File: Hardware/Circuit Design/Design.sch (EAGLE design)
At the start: 41 parts, among them J1 6495, U1 ATMEGA328-PU, U2 TP4056, U3 HTU21D, U4 MT3608, Y1 16 MHz HC-49US

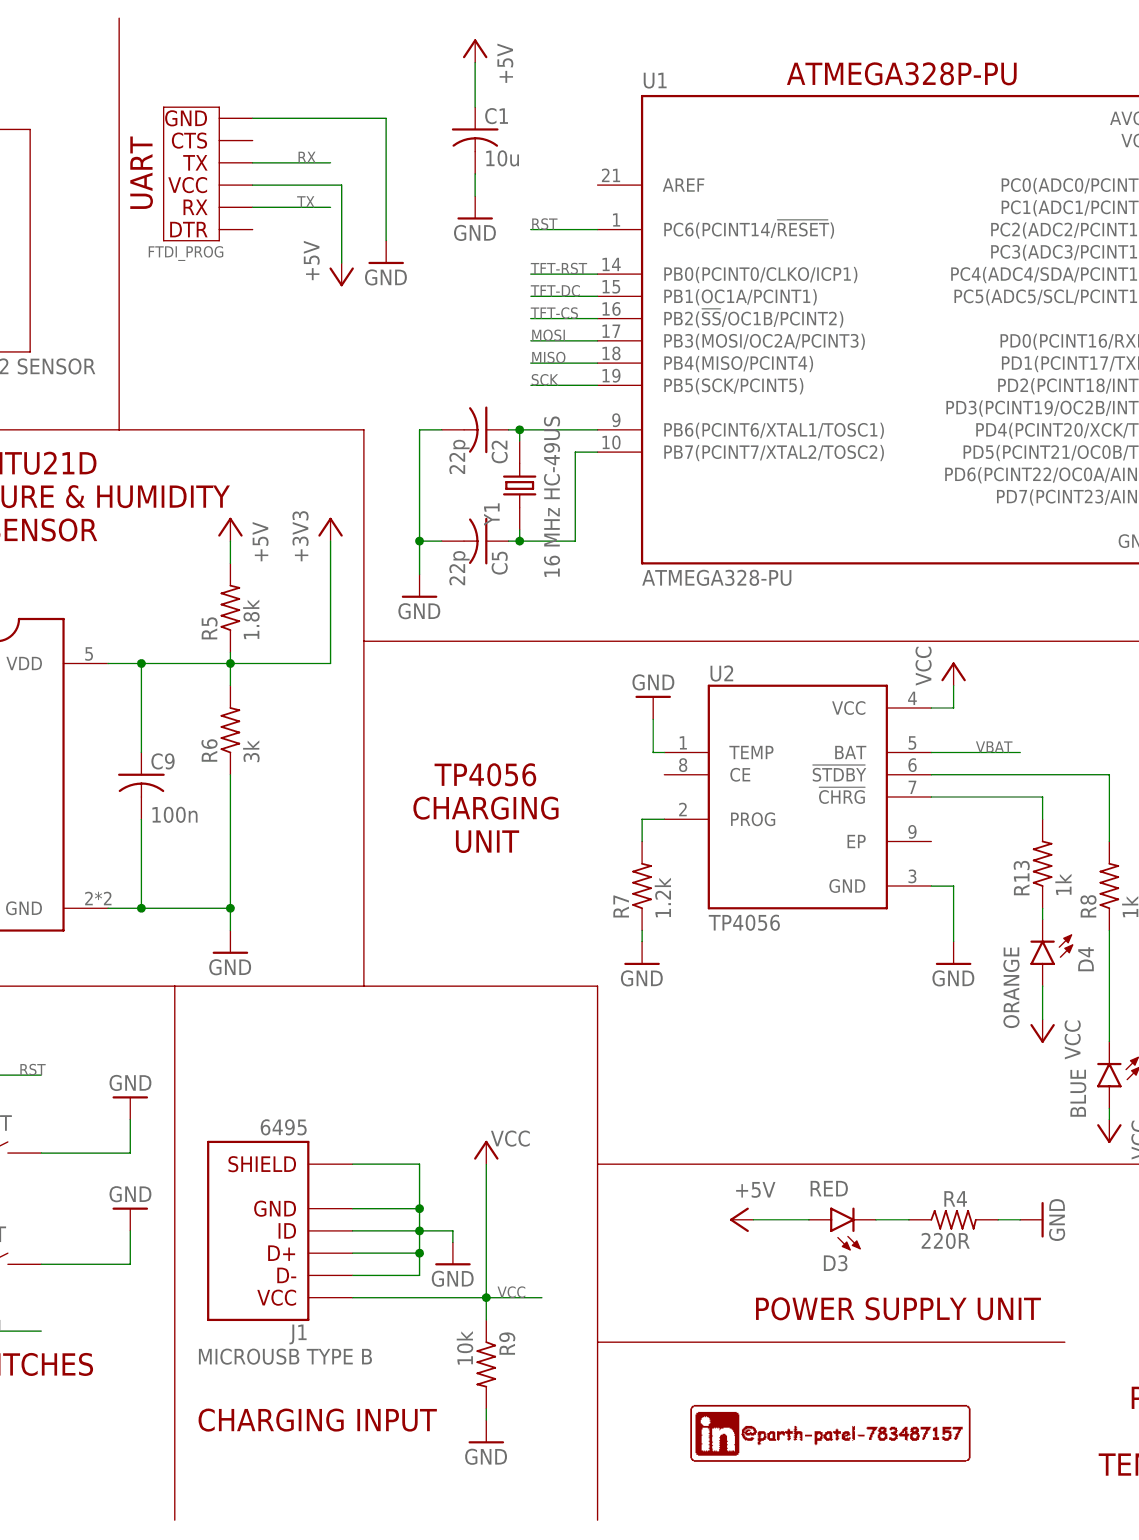
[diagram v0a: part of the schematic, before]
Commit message: Design display for co2 monitor
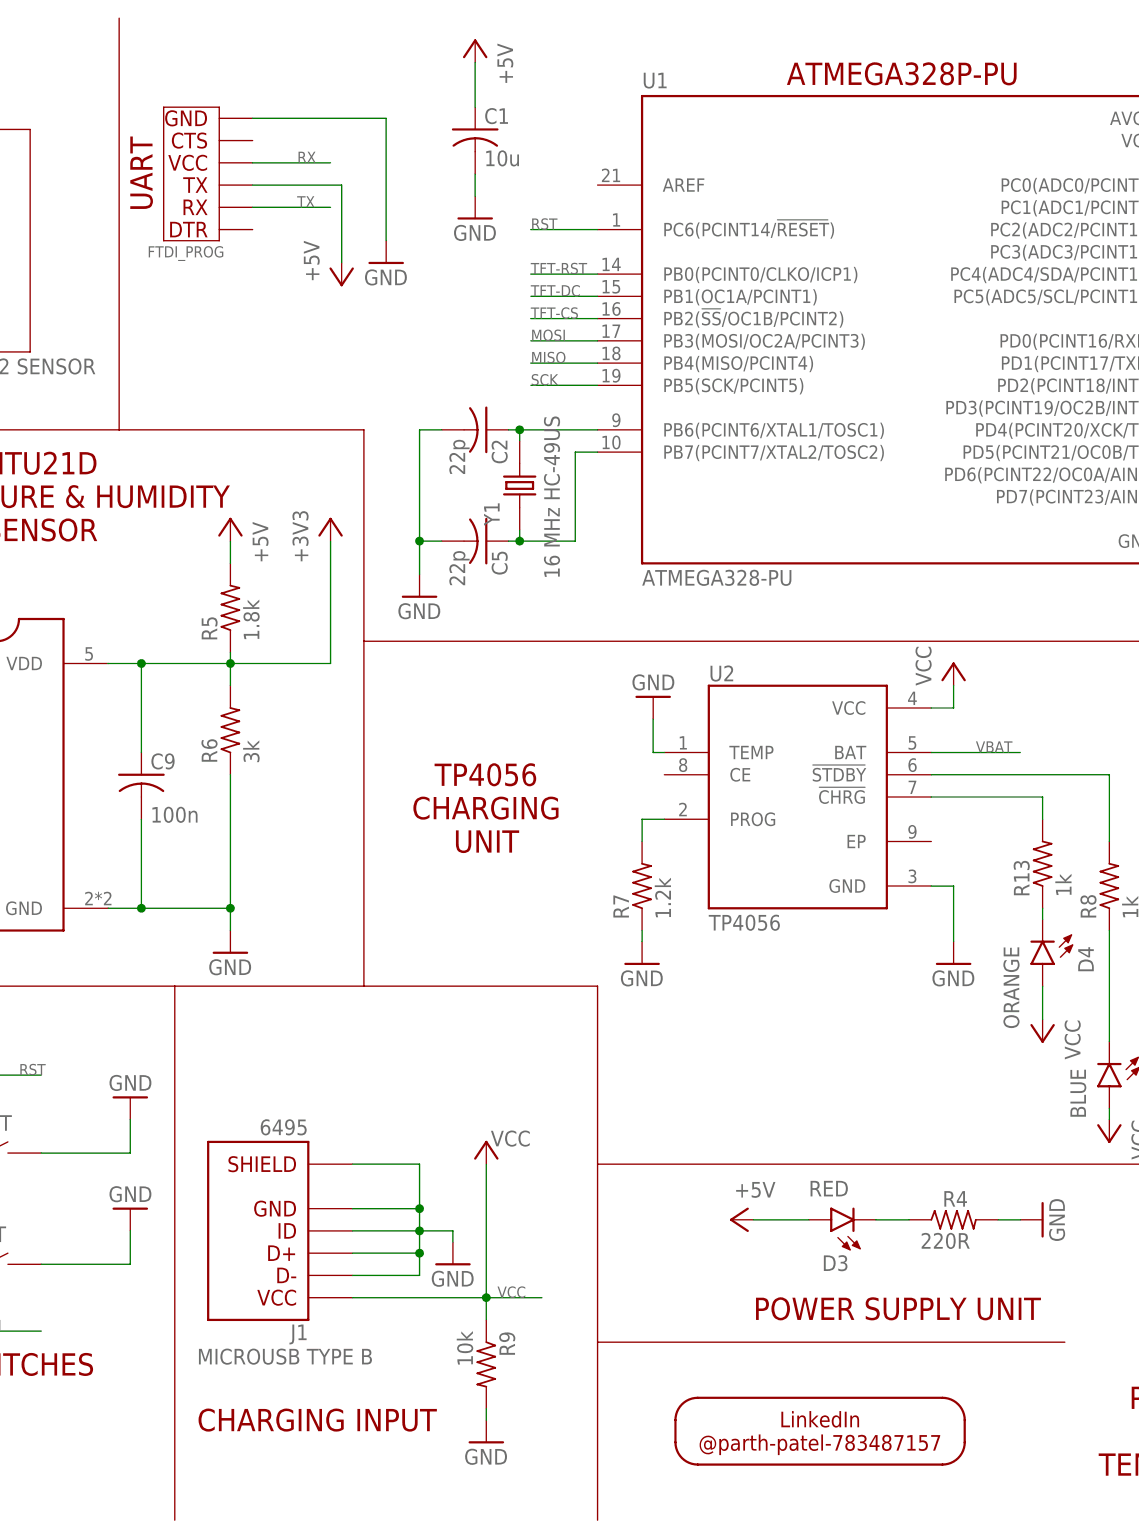
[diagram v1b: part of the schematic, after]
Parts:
- added U$2: LOGO, PCB Logo:LOGO
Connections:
- net +5V: now also FTDI_PROG.TX; no longer FTDI_PROG.VCC
- net RX: now also FTDI_PROG.VCC; no longer FTDI_PROG.TX

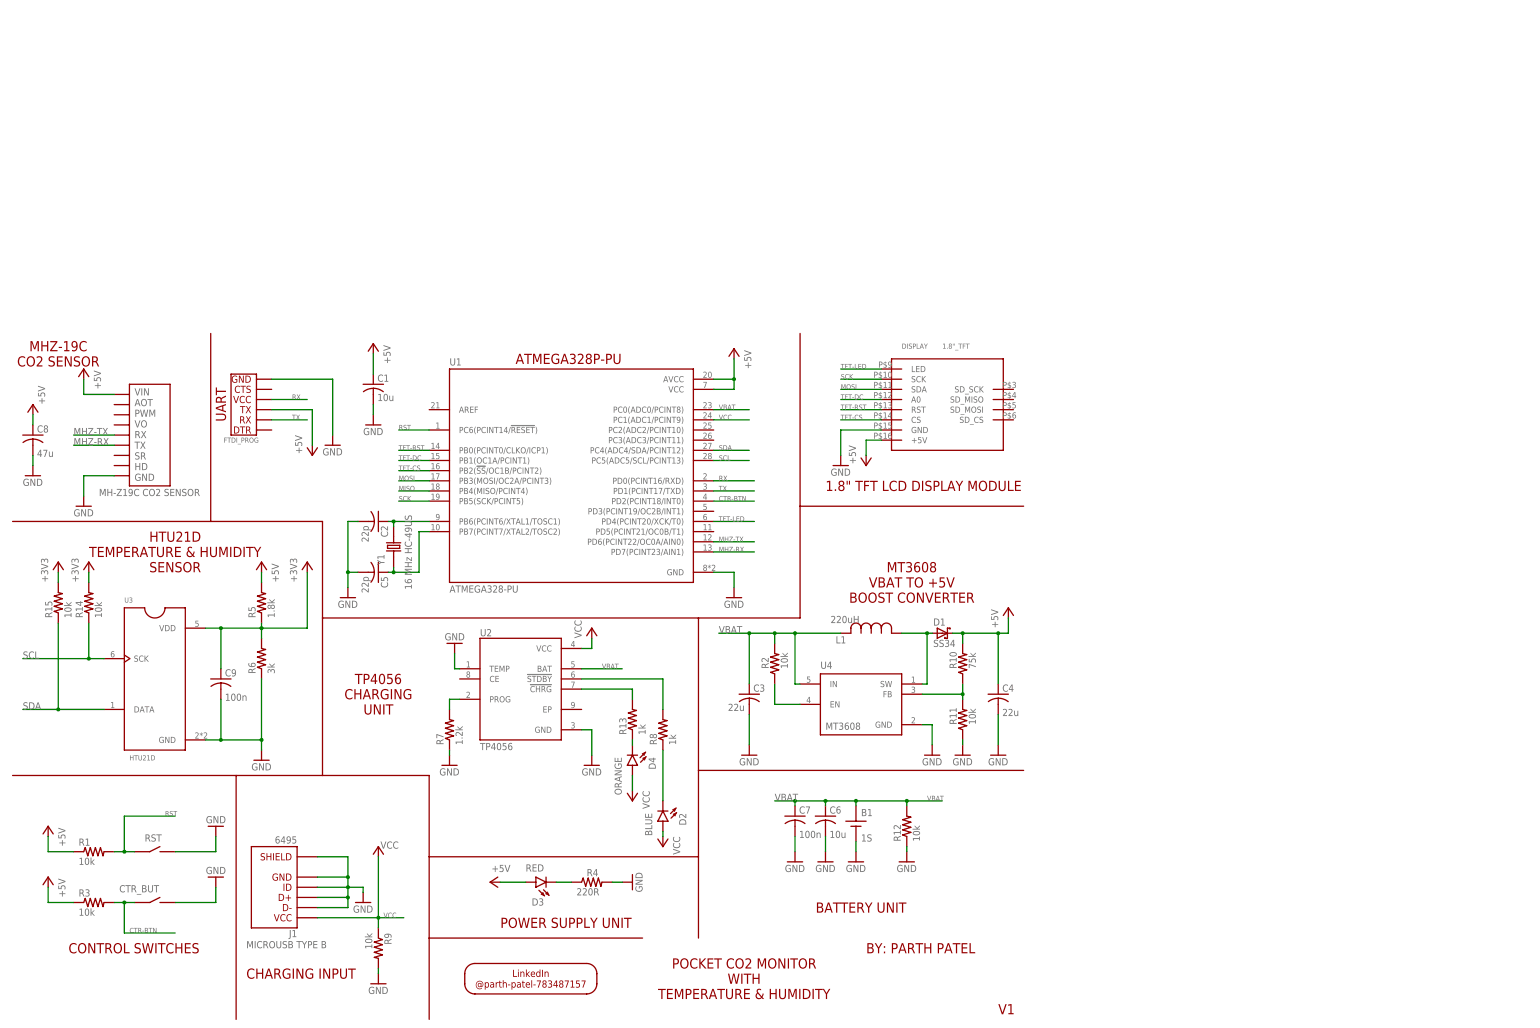
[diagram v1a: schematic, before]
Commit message: Correct the sleep mode enter function and add the new board design
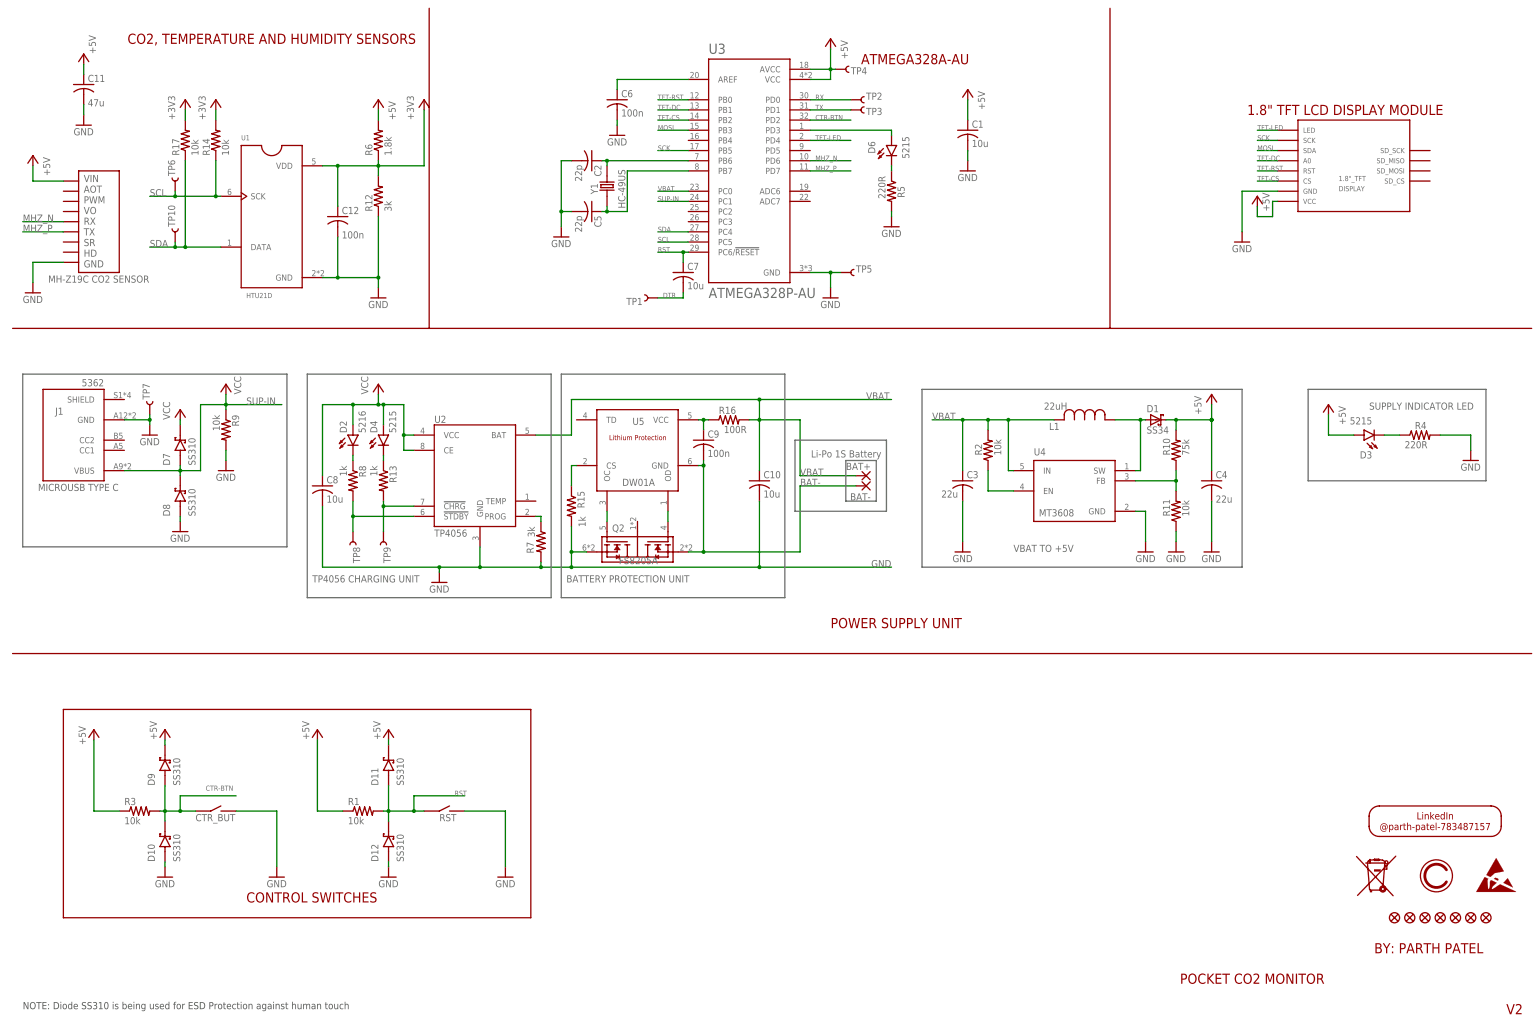
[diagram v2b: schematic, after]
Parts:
- removed B1: 1S, 18650 1S PCB Mount:DIP-1S-18650
- removed FTDI_PROG: UART, FTDI Adapter:UART
- added BAT+, BAT-: WIREPADSMD5-2,5, wirepad:WIREPADSMD5-2,5
- added C10: 10u, rcl:C-USC0805
- added C11: 47u, rcl:C-USC0805
- added C12: 100n, rcl:C-USC0805
- added D10, D11, D12, D7, D8, D9: SS310, Schottky SS310:SS310
- added D6: 5215, led:LEDCHIP-LED0603
- added FID1, FID2, FID3, FID4, FID5, FID6, FID7: FIDUCIAL"", Airquality_Sensor:FIDUCIAL""
- added Q2: FS8205A, FS8205A:FS8205A
- added R16: 100R, rcl:R-US_R0805
- added R17: 10k, rcl:R-US_R0805
- added TP1, TP10, TP2, TP3, TP4, TP5, TP6, TP7: TEST-POINT3, SparkFun-Connectors:TEST-POINT3
- added TP8: ~STDBY, SparkFun-Connectors:TEST-POINT3
- added TP9: ~CHRG, SparkFun-Connectors:TEST-POINT3
- added U5: DW01A, DW01A:DW01A
- C6: value 10u -> 100n
- C7: value 100n -> 10u
- C8: value 47u -> 10u
- CTR_BUT, RST: value 4.5X4.5-SMD-TACTILE-SWITCH -> 7058; device Switches:4.5X4.5-SMD-TACTILE-SWITCH -> Switches:DIP_3X6MM_SIDE_PRESS_2PIN
- D2: value BLUE -> 5216
- D3: value RED -> 5215
- D4: value ORANGE -> 5215
- J1: value 6495 -> 5362; device MicroUSB Type B Socket:10103593-0001LF -> MicroUSB Type C Socket:6_PIN_TYPE_C_FEMALE
- L1: value 220uH -> 22uH
- R12: value 10k -> 3k
- R15: value 10k -> 1k
- R5: value 1.8k -> 220R
- R6: value 3k -> 1.8k
- R7: value 1.2k -> 3k
- U$1: value MH-Z19C -> LOGO_17MM; device MH-Z19 Sensor:MH-Z19C -> PCB Logo:LOGO_17MM
- U$2: value LOGO -> MH-Z19C; device PCB Logo:LOGO -> MH-Z19 Sensor:MH-Z19C
- U1: value ATMEGA328-PU -> HTU21D; device ATMEGA328-PU:ATMEGA328-PU -> HTU21D:HTU21D
- U3: value HTU21D -> ATMEGA328P-AU; device HTU21D:HTU21D -> ATMEGA328P-AU:ATMEGA328P-AU
- Y1: value 16 MHz HC-49US -> HC-49US
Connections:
- removed net MHZ-RX: U$1.TX, U1.PD7(PCINT23/AIN1)
- removed net MHZ-TX: U$1.RX, U1.PD6(PCINT22/OC0A/AIN0)
- removed net MISO: U1.PB4(MISO/PCINT4)
- removed net N$1: R8.2, U2.!STDBY
- removed net N$4: R7.2, U2.PROG
- new net BAT-: BAT-.P, C9.2, Q2.S1, U5.GND
- new net DTR: C7.2, TP1.1
- new net MHZ_N: U$2.RX, U3.PD6
- new net MHZ_P: U$2.TX, U3.PD7
- new net N$13: D6.C, R5.1
- new net N$14: D6.A, U3.PD3
- new net N$15: Q2.G2, U5.OC
- new net N$16: R13.2, TP9.1, U2.!CHRG
- new net N$17: R8.2, TP8.1, U2.!STDBY
- new net N$18: R7.1, U2.PROG
- new net N$19: Q2.G1, U5.OD
- new net N$20: R15.1, U5.CS
- new net N$21: C9.1, R16.1, U5.VCC
- new net SUP-IN: D7.A, D8.K, J1.VBUS, R9.1, U3.PC1
- net +3V3: now also C12.1, R12.2, R17.2, R6.1, U1.VDD; no longer C9.1, R15.2, R5.1, R6.2, U3.VDD
- net +5V: now also C11.1, D11.K, D9.K, R6.2, TP4.1, U$2.VIN, U3.AVCC, U3.VCC; no longer C8.1, FTDI_PROG.TX, R5.2, U$1.VIN, U1.AVCC, U1.VCC
- net CTR-BTN: now also D10.K, D9.A, U3.PD2; no longer U1.PD2(PCINT18/INT0)
- net GND: now also C10.2, C11.2, C12.2, D10.A, D12.A, D8.A, J1.GND, Q2.S2, R15.2, R5.2, R7.2, TP5.1, TP7.1, U$2.GND; no longer B1.V-, C7.2, C9.2, FTDI_PROG.GND, J1.2, J1.3, J1.4, J1.5, J1.SHIELD, R6.1, R7.1, U$1.GND, U2.TEMP
- net MOSI: now also U3.PB3; no longer U1.PB3(MOSI/OC2A/PCINT3)
- net N$10: now also U3.PB6; no longer U1.PB6(PCINT6/XTAL1/TOSC1)
- net N$2: now also U3.PB7; no longer U1.PB7(PCINT7/XTAL2/TOSC2)
- net N$6: now also C6.1, U3.AREF; no longer R13.2, U2.!CHRG
- net RST: now also C7.1, D11.A, D12.K, U3.PC6/!RESET; no longer U1.PC6(PCINT14/!RESET!)
- net RX: now also TP2.1, U3.PD0; no longer FTDI_PROG.VCC, U1.PD0(PCINT16/RXD)
- net SCK: now also U3.PB5; no longer U1.PB5(SCK/PCINT5)
- net SCL: now also TP6.1, U1.SCK, U3.PC5; no longer U1.PC5(ADC5/SCL/PCINT13), U3.SCK
- net SDA: now also R17.1, TP10.1, U1.DATA, U3.PC4; no longer R15.1, U1.PC4(ADC4/SDA/PCINT12), U3.DATA
- net TFT-CS: now also U3.PB2; no longer U1.PB2(!SS!/OC1B/PCINT2)
- net TFT-DC: now also U3.PB1; no longer U1.PB1(OC1A/PCINT1)
- net TFT-LED: now also U3.PD4; no longer U1.PD4(PCINT20/XCK/T0)
- net TFT-RST: now also U3.PB0; no longer U1.PB0(PCINT0/CLKO/ICP1)
- net TX: now also TP3.1, U3.PD1; no longer FTDI_PROG.RX, U1.PD1(PCINT17/TXD)
- net VBAT: now also BAT+.P, C10.1, R16.2, U3.PC0; no longer B1.V+, C6.1, C7.1, R12.2, U1.PC0(ADC0/PCINT8)
- net VCC: now also C8.1, D7.K, U2.CE; no longer J1.1, R9.1, U1.PC1(ADC1/PCINT9)
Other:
- note added: "ATMEGA328A-AU"
- note added: "BATTERY PROTECTION UNIT"
- note added: "CO2, TEMPERATURE AND HUMIDITY SENSORS"
- note added: "Li-Po 1S Battery"
- note added: "MICROUSB TYPE C"
- note added: "NOTE: Diode SS310 is being used for ESD Protection against human touch"
- note added: "POCKET CO2 MONITOR"
- note added: "SUPPLY INDICATOR LED"
- note added: "V2"
- note added: "VBAT TO +5V"
- note removed: "ATMEGA328P-PU"
- note removed: "BATTERY UNIT"
- note removed: "CHARGING INPUT"
- note removed: "HTU21D TEMPERATURE & HUMIDITY SENSOR"
- note removed: "MHZ-19C CO2 SENSOR"
- note removed: "MICROUSB TYPE B"
- note removed: "MT3608 VBAT TO +5V BOOST CONVERTER"
- note removed: "POCKET CO2 MONITOR WITH TEMPERATURE & HUMIDITY"
- note removed: "V1"
- moved on the sheet: C1, C2, C3, C4, C5, C6, C7, C8, C9, CTR_BUT, D1, D2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

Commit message: Change Mounting Holes size from M1.5 to M4
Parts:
- removed FID6, FID7: FIDUCIAL"", Airquality_Sensor:FIDUCIAL""
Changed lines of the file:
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@@
 <part name="FID4" library="Airquality_Sensor" library_urn="urn:adsk.eagle:library:16015176" deviceset="FIDUCIAL" device="&quot;&quot;" package3d_urn="urn:adsk.eagle:package:15955190/2"/>
 <part name="FID5" library="Airquality_Sensor" library_urn="urn:adsk.eagle:library:16015176" deviceset="FIDUCIAL" device="&quot;&quot;" package3d_urn="urn:adsk.eagle:package:15955190/2"/>
-<part name="FID6" library="Airquality_Sensor" library_urn="urn:adsk.eagle:library:16015176" deviceset="FIDUCIAL" device="&quot;&quot;" package3d_urn="urn:adsk.eagle:package:15955190/2"/>
-<part name="FID7" library="Airquality_Sensor" library_urn="urn:adsk.eagle:library:16015176" deviceset="FIDUCIAL" device="&quot;&quot;" package3d_urn="urn:adsk.eagle:package:15955190/2"/>
 <part name="LOGO1" library="logo" library_urn="urn:adsk.eagle:library:264" deviceset="ESD_10.00" device=""/>
 <part name="LOGO2" library="logo" library_urn="urn:adsk.eagle:library:264" deviceset="COPYRIGHT-8MM" device=""/>
@@
 <instance part="FID4" gate="G$1" x="360.68" y="29.21" smashed="yes" rot="R180"/>
 <instance part="FID5" gate="G$1" x="356.87" y="29.21" smashed="yes" rot="R180"/>
-<instance part="FID6" gate="G$1" x="353.06" y="29.21" smashed="yes" rot="R180"/>
-<instance part="FID7" gate="G$1" x="349.25" y="29.21" smashed="yes" rot="R180"/>
 <instance part="LOGO1" gate="G$1" x="369.57" y="35.56" smashed="yes"/>
 <instance part="LOGO2" gate="G$1" x="355.6" y="35.56" smashed="yes"/>
